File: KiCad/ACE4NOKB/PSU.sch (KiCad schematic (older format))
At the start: 30 parts

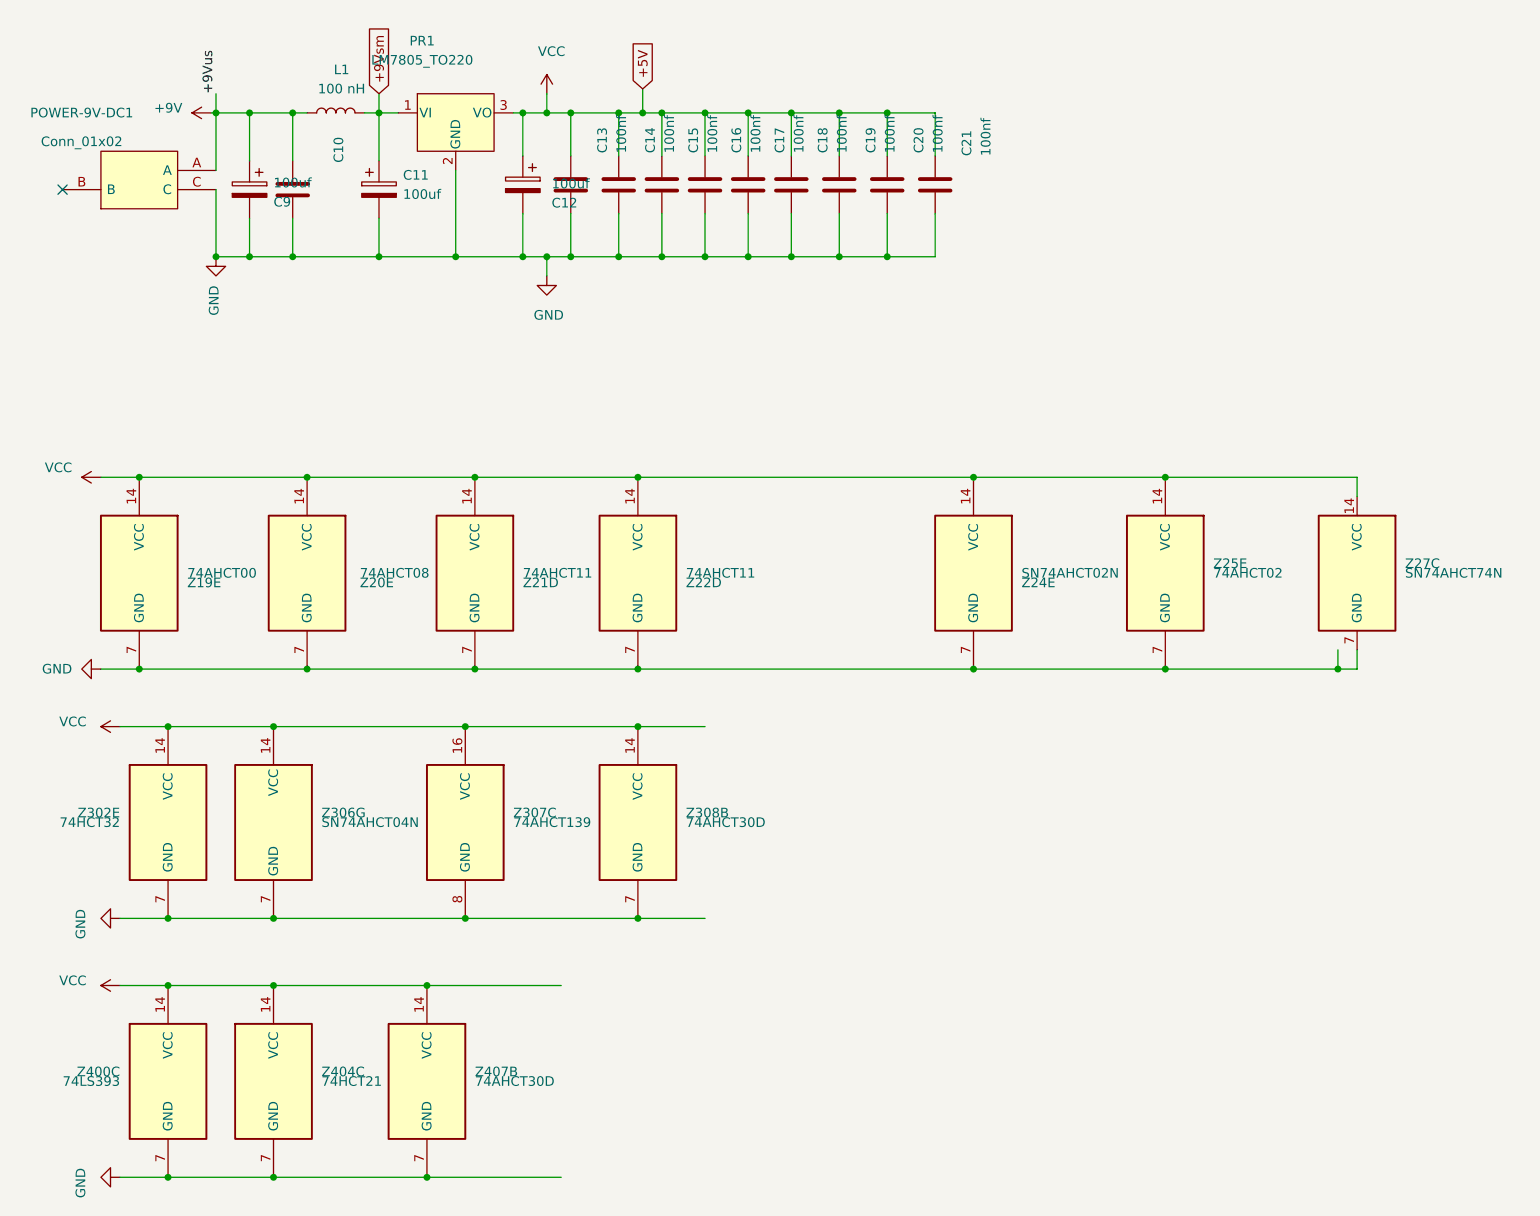
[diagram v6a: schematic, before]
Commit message: Fix several problems with Chip Select. Reconnect the Data bus for the VDG to the CPU bus which has become disconnected.
Signed-off-by: John Bradley <flypie@rocketmail.com>
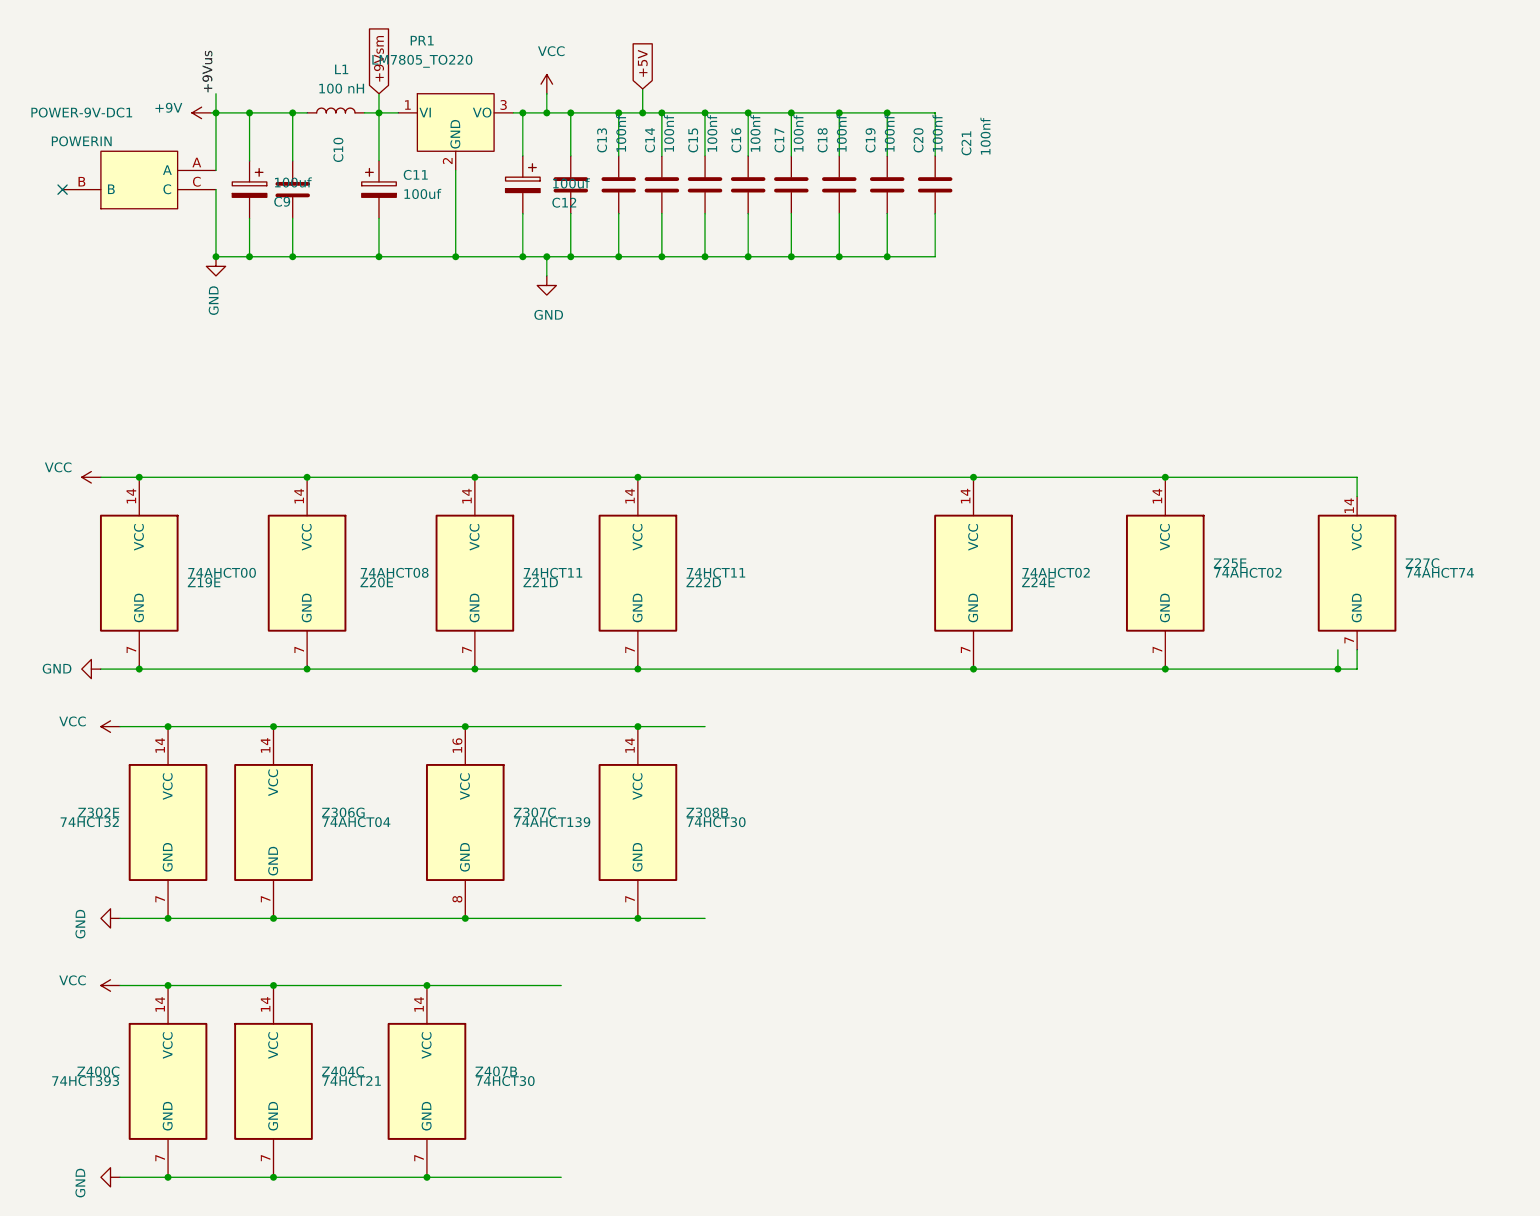
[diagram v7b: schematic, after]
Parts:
- C11: footprint Capacitor_THT:CP_Radial_D4.0mm_P1.50mm -> Capacitor_THT:CP_Radial_D5.0mm_P2.00mm; Manufacturer_Name Vishay -> Wurth Elektronik; Manufacturer_Part_Number K104K10X7RF53H5 -> 860010372006
- C12, C9: Manufacturer_Name (none) -> Wurth Elektronik; Manufacturer_Part_Number (none) -> 860010372006
- L1: Manufacturer_Name (none) -> KEMET; Manufacturer_Part_Number (none) -> SBT-0260TF
- POWER-9V-DC1: value Conn_01x02 -> POWERIN; Manufacturer_Name (none) -> Kobiconn; Manufacturer_Part_Number (none) -> 163-179PH-EX
- PR1: Manufacturer_Name (none) -> Texas Instruments; Manufacturer_Part_Number (none) -> LM7805CT/NOPB
- Z19: Manufacturer_Name (none) -> Texas Instruments; Manufacturer_Part_Number (none) -> SN74AHCT00NE4
- Z20: Manufacturer_Name (none) -> Texas Instruments; Manufacturer_Part_Number (none) -> SN74AHCT08N
- Z21, Z22: value 74AHCT11 -> 74HCT11; Manufacturer_Name (none) -> Texas Instruments; Manufacturer_Part_Number (none) -> CD74HCT11M
- Z24: value SN74AHCT02N -> 74AHCT02; Manufacturer_Name (none) -> Texas Instruments; Manufacturer_Part_Number (none) -> SN74AHCT02N
- Z25: Manufacturer_Name (none) -> Texas Instruments; Manufacturer_Part_Number (none) -> SN74AHCT02N
- Z27: value SN74AHCT74N -> 74AHCT74; Manufacturer_Name (none) -> Texas Instruments; Manufacturer_Part_Number (none) -> SN74AHCT74N
- Z302: Manufacturer_Name (none) -> Texas Instruments; Manufacturer_Part_Number (none) -> SN74HCT32NE4
- Z306: value SN74AHCT04N -> 74AHCT04; Manufacturer_Name (none) -> Texas Instruments; Manufacturer_Part_Number (none) -> SN74AHCT04N
- Z307: Manufacturer_Name (none) -> Texas Instruments; Manufacturer_Part_Number (none) -> SN74AHCT139N
- Z308, Z407: value 74AHCT30D -> 74HCT30; Manufacturer_Name NEXPERIA -> Texas Instruments; Manufacturer_Part_Number 74AHCT30D -> CD74HC30E
- Z400: value 74LS393 -> 74HCT393; Manufacturer_Name (none) -> Texas Instruments; Manufacturer_Part_Number (none) -> CD74HCT393E
- Z404: Manufacturer_Name (none) -> Texas Instruments; Manufacturer_Part_Number (none) -> CD74HCT21E
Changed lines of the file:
@@
 P 600 1500
 F 0 "POWER-9V-DC1" H 700 1100 50  0000 C CNN
-F 1 "Conn_01x02" H 700 1250 50  0000 C CNN
+F 1 "POWERIN" H 700 1250 50  0000 C CNN
 F 2 "SamacSys_Parts:163179PHEX" H 600 1500 50  0001 C CNN
 F 3 "" H 600 1500 50  0001 C CNN
+F 4 "Kobiconn" H 600 1500 50  0001 C CNN "Manufacturer_Name"
+F 5 "163-179PH-EX " H 600 1500 50  0001 C CNN "Manufacturer_Part_Number"
 	1    600  1500
 	1    0    0    1
@@
 P 7350 3500
 F 0 "Z27" H 7100 3550 50  0000 R CNN
-F 1 "SN74AHCT74N" H 7100 3500 50  0000 R CNN
+F 1 "74AHCT74" H 7100 3500 50  0000 R CNN
 F 2 "Package_DIP:DIP-14_W7.62mm_Socket" H 7350 3500 50  0001 C CNN
 F 3 "74xx/74hc_hct74.pdf" H 7350 3500 50  0001 C CNN
+F 4 "Texas Instruments" H 7350 3500 50  0001 C CNN "Manufacturer_Name"
+F 5 "SN74AHCT74N" H 7350 3500 50  0001 C CNN "Manufacturer_Part_Number"
 	3    7350 3500
 	-1   0    0    -1
@@
 P 2500 6150
 F 0 "Z407" H 2250 6200 50  0000 R CNN
-F 1 "74AHCT30D" H 2250 6150 50  0000 R CNN
+F 1 "74HCT30" H 2250 6150 50  0000 R CNN
 F 2 "Package_DIP:DIP-14_W7.62mm_Socket" H 2500 6150 50  0001 C CNN
 F 3 "http://www.ti.com/lit/gpn/sn74LS21" H 2500 6150 50  0001 C CNN
-F 4 "NEXPERIA" H 2500 6150 50  0001 C CNN "Manufacturer_Name"
-F 5 "74AHCT30D" H 2500 6150 50  0001 C CNN "Manufacturer_Part_Number"
+F 4 "Texas Instruments" H 2500 6150 50  0001 C CNN "Manufacturer_Name"
+F 5 "CD74HC30E" H 2500 6150 50  0001 C CNN "Manufacturer_Part_Number"
 	2    2500 6150
 	-1   0    0    -1
@@
 F 2 "Package_DIP:DIP-16_W7.62mm_Socket" H 2700 4800 50  0001 C CNN
 F 3 "http://www.ti.com/lit/gpn/sn74LS139" H 2700 4800 50  0001 C CNN
+F 4 "Texas Instruments" H 2700 4800 50  0001 C CNN "Manufacturer_Name"
+F 5 "SN74AHCT139N " H 2700 4800 50  0001 C CNN "Manufacturer_Part_Number"
 	3    2700 4800
 	-1   0    0    -1
@@
 P 3600 3500
 F 0 "Z22" H 3350 3450 50  0000 R CNN
-F 1 "74AHCT11" H 3350 3500 50  0000 R CNN
+F 1 "74HCT11" H 3350 3500 50  0000 R CNN
 F 2 "Package_DIP:DIP-14_W7.62mm_Socket" H 3600 3500 50  0001 C CNN
 F 3 "http://www.ti.com/lit/gpn/sn74LS11" H 3600 3500 50  0001 C CNN
+F 4 "Texas Instruments" H 3600 3500 50  0001 C CNN "Manufacturer_Name"
+F 5 "CD74HCT11M" H 3600 3500 50  0001 C CNN "Manufacturer_Part_Number"
 	4    3600 3500
 	-1   0    0    -1
@@
 F 2 "Capacitor_THT:CP_Radial_D5.0mm_P2.00mm" H 3038 1325 50  0001 C CNN
 F 3 "" H 3000 1475 50  0001 C CNN
+F 4 "Wurth Elektronik" H 3000 1475 50  0001 C CNN "Manufacturer_Name"
+F 5 "860010372006" H 3000 1475 50  0001 C CNN "Manufacturer_Part_Number"
 	1    3000 1475
 	-1   0    0    -1
@@
 F 2 "SamacSys_Parts:KEMET_SBT_0260T" H 2025 1100 50  0001 C CNN
 F 3 "" H 2025 1100 50  0001 C CNN
+F 4 "KEMET" H 2025 1100 50  0001 C CNN "Manufacturer_Name"
+F 5 "SBT-0260TF" H 2025 1100 50  0001 C CNN "Manufacturer_Part_Number"
 	1    2025 1100
 	0    -1   -1   0
@@
 P 5350 3500
 F 0 "Z24" H 5100 3450 50  0000 R CNN
-F 1 "SN74AHCT02N" H 5100 3500 50  0000 R CNN
+F 1 "74AHCT02" H 5100 3500 50  0000 R CNN
 F 2 "Package_DIP:DIP-14_W7.62mm_Socket" H 5350 3500 50  0001 C CNN
 F 3 "http://www.ti.com/lit/gpn/sn74ls02" H 5350 3500 50  0001 C CNN
+F 4 "Texas Instruments" H 5350 3500 50  0001 C CNN "Manufacturer_Name"
+F 5 "SN74AHCT02N" H 5350 3500 50  0001 C CNN "Manufacturer_Part_Number"
 	5    5350 3500
 	-1   0    0    -1
@@
 F 2 "Package_TO_SOT_THT:TO-220-3_Vertical" H 2450 1225 50  0001 C CIN
 F 3 "http://www.fairchildsemi.com/ds/LM/LM7805.pdf" H 2450 950 50  0001 C CNN
+F 4 "Texas Instruments" H 2450 1000 50  0001 C CNN "Manufacturer_Name"
+F 5 "LM7805CT/NOPB" H 2450 1000 50  0001 C CNN "Manufacturer_Part_Number"
 	1    2450 1000
 	1    0    0    -1
@@
 F 2 "Package_DIP:DIP-14_W7.62mm_Socket" H 1000 3500 50  0001 C CNN
 F 3 "http://www.ti.com/lit/gpn/sn74ls00" H 1000 3500 50  0001 C CNN
+F 4 "Texas Instruments" H 1000 3500 50  0001 C CNN "Manufacturer_Name"
+F 5 "SN74AHCT00NE4" H 1000 3500 50  0001 C CNN "Manufacturer_Part_Number"
 	5    1000 3500
 	-1   0    0    -1
@@
 P 2750 3500
 F 0 "Z21" H 2500 3450 50  0000 R CNN
-F 1 "74AHCT11" H 2500 3500 50  0000 R CNN
+F 1 "74HCT11" H 2500 3500 50  0000 R CNN
 F 2 "Package_DIP:DIP-14_W7.62mm_Socket" H 2750 3500 50  0001 C CNN
 F 3 "http://www.ti.com/lit/gpn/sn74LS11" H 2750 3500 50  0001 C CNN
+F 4 "Texas Instruments" H 2750 3500 50  0001 C CNN "Manufacturer_Name"
+F 5 "CD74HCT11M" H 2750 3500 50  0001 C CNN "Manufacturer_Part_Number"
 	4    2750 3500
 	-1   0    0    -1
@@
 F 2 "Package_DIP:DIP-14_W7.62mm_Socket" H 6350 3500 50  0001 C CNN
 F 3 "http://www.ti.com/lit/gpn/sn74ls02" H 6350 3500 50  0001 C CNN
+F 4 "Texas Instruments" H 6350 3500 50  0001 C CNN "Manufacturer_Name"
+F 5 "SN74AHCT02N" H 6350 3500 50  0001 C CNN "Manufacturer_Part_Number"
 	5    6350 3500
 	-1   0    0    -1
@@
 P 1700 4800
 F 0 "Z306" H 1450 4850 50  0000 R CNN
-F 1 "SN74AHCT04N" H 1450 4800 50  0000 R CNN
+F 1 "74AHCT04" H 1450 4800 50  0000 R CNN
 F 2 "Package_DIP:DIP-14_W7.62mm_Socket" H 1700 4800 50  0001 C CNN
 F 3 "http://www.ti.com/lit/gpn/sn74LS04" H 1700 4800 50  0001 C CNN
+F 4 "Texas Instruments" H 1700 4800 50  0001 C CNN "Manufacturer_Name"
+F 5 "SN74AHCT04N" H 1700 4800 50  0001 C CNN "Manufacturer_Part_Number"
 	7    1700 4800
 	-1   0    0    -1
@@
 F 0 "C11" H 2375 1575 50  0000 L CNN
 F 1 "100uf" H 2375 1475 50  0000 L CNN
-F 2 "Capacitor_THT:CP_Radial_D4.0mm_P1.50mm" H 2600 1550 50  0001 L CNN
+F 2 "Capacitor_THT:CP_Radial_D5.0mm_P2.00mm" H 2600 1550 50  0001 L CNN
 F 3 "" H 2600 1450 50  0001 L CNN
 F 4 "Vishay 100nF Multilayer Ceramic Capacitor MLCC 50V dc +~-10% X7R Dielectric Radial, Max. Temp. +125C" H 2600 1350 50  0001 L CNN "Description"
@@
 F 6 "8523267" H 2600 1150 50  0001 L CNN "RS Part Number"
 F 7 "http:/uk.rs-online.com/web/p/products/8523267" H 2600 1050 50  0001 L CNN "RS Price/Stock"
-F 8 "Vishay" H 2600 950 50  0001 L CNN "Manufacturer_Name"
-F 9 "K104K10X7RF53H5" H 2600 850 50  0001 L CNN "Manufacturer_Part_Number"
+F 8 "Wurth Elektronik" H 2600 950 50  0001 L CNN "Manufacturer_Name"
+F 9 "860010372006" H 2600 850 50  0001 L CNN "Manufacturer_Part_Number"
 F 10 "70122995" H 2600 750 50  0001 L CNN "Allied_Number"
 	1    2250 1500
@@
 F 2 "Capacitor_THT:CP_Radial_D5.0mm_P2.00mm" H 1613 1350 50  0001 C CNN
 F 3 "" H 1575 1500 50  0001 C CNN
+F 4 "Wurth Elektronik" H 1575 1500 50  0001 C CNN "Manufacturer_Name"
+F 5 "860010372006" H 1575 1500 50  0001 C CNN "Manufacturer_Part_Number"
 	1    1575 1500
 	-1   0    0    -1
@@
 F 2 "Package_DIP:DIP-14_W7.62mm_Socket" H 1875 3500 50  0001 C CNN
 F 3 "http://www.ti.com/lit/gpn/sn74LS08" H 1875 3500 50  0001 C CNN
+F 4 "Texas Instruments" H 1875 3500 50  0001 C CNN "Manufacturer_Name"
+F 5 "SN74AHCT08N" H 1875 3500 50  0001 C CNN "Manufacturer_Part_Number"
 	5    1875 3500
 	-1   0    0    -1
@@
 P 3600 4800
 F 0 "Z308" H 3350 4850 50  0000 R CNN
-F 1 "74AHCT30D" H 3350 4800 50  0000 R CNN
+F 1 "74HCT30" H 3350 4800 50  0000 R CNN
 F 2 "Package_DIP:DIP-14_W7.62mm_Socket" H 3600 4800 50  0001 C CNN
 F 3 "http://www.ti.com/lit/gpn/sn74LS30" H 3600 4800 50  0001 C CNN
-F 4 "NEXPERIA" H 3600 4800 50  0001 C CNN "Manufacturer_Name"
-F 5 "74AHCT30D" H 3600 4800 50  0001 C CNN "Manufacturer_Part_Number"
+F 4 "Texas Instruments" H 3600 4800 50  0001 C CNN "Manufacturer_Name"
+F 5 "CD74HC30E" H 3600 4800 50  0001 C CNN "Manufacturer_Part_Number"
 	2    3600 4800
 	-1   0    0    -1
@@
 F 2 "Package_DIP:DIP-14_W7.62mm_Socket" H 1150 4800 50  0001 C CNN
 F 3 "http://www.ti.com/lit/gpn/sn74LS32" H 1150 4800 50  0001 C CNN
+F 4 "Texas Instruments" H 1150 4800 50  0001 C CNN "Manufacturer_Name"
+F 5 "SN74HCT32NE4" H 1150 4800 50  0001 C CNN "Manufacturer_Part_Number"
 	5    1150 4800
 	1    0    0    -1
@@
 F 2 "Package_DIP:DIP-14_W7.62mm_Socket" H 1700 6150 50  0001 C CNN
 F 3 "74xx\\74LS393.pdf" H 1700 6150 50  0001 C CNN
+F 4 "Texas Instruments" H 1700 6150 50  0001 C CNN "Manufacturer_Name"
+F 5 "CD74HCT21E" H 1700 6150 50  0001 C CNN "Manufacturer_Part_Number"
 	3    1700 6150
 	1    0    0    -1
@@
 P 1150 6150
 F 0 "Z400" H 900 6200 50  0000 R CNN
-F 1 "74LS393" H 900 6150 50  0000 R CNN
+F 1 "74HCT393" H 900 6150 50  0000 R CNN
 F 2 "Package_DIP:DIP-14_W7.62mm_Socket" H 1150 6150 50  0001 C CNN
 F 3 "74xx\\74LS393.pdf" H 1150 6150 50  0001 C CNN
+F 4 "Texas Instruments" H 1150 6150 50  0001 C CNN "Manufacturer_Name"
+F 5 "CD74HCT393E " H 1150 6150 50  0001 C CNN "Manufacturer_Part_Number"
 	3    1150 6150
 	1    0    0    -1
